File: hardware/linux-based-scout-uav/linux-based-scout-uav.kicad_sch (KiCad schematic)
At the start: 0 parts

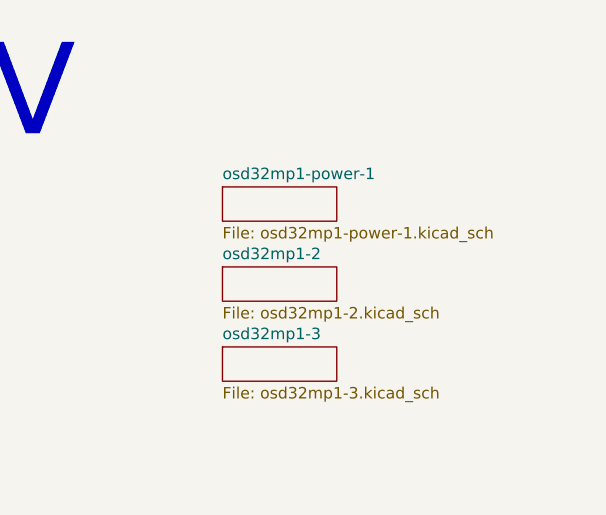
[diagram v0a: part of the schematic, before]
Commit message: Schematic update
Schematic updates on battery connector and OSD32MP1 power section.
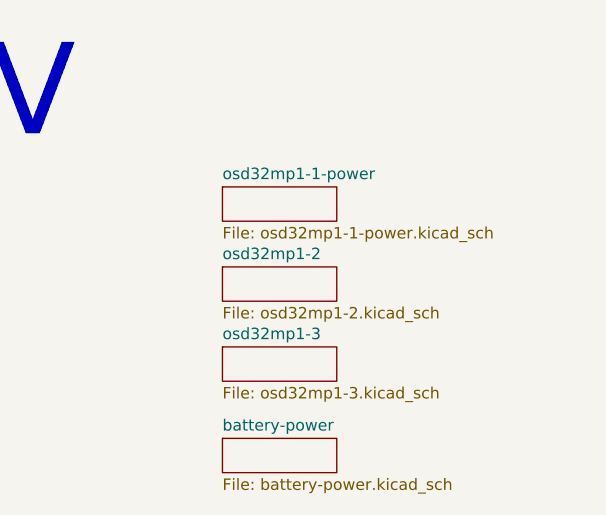
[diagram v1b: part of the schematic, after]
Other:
- sheet osd32mp1-power-1 renamed osd32mp1-1-power
- added sheet battery-power (battery-power.kicad_sch)
- sheet osd32mp1-1-power: file osd32mp1-power-1.kicad_sch -> osd32mp1-1-power.kicad_sch
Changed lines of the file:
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@@
+	)
+	(sheet
+		(at 242.57 59.69)
+		(size 12.7 3.81)
+		(fields_autoplaced yes)
+		(stroke
+			(width 0.1524)
+			(type solid)
+		)
+		(fill
+			(color 0 0 0 0.0000)
+		)
+		(property "Sheetname" "battery-power"
+			(at 242.57 58.9784 0)
+			(show_name yes)
+			(effects
+				(font
+					(size 1.27 1.27)
+				)
+				(justify left bottom)
+			)
+		)
+		(property "Sheetfile" "battery-power.kicad_sch"
+			(at 242.57 64.0846 0)
+			(effects
+				(font
+					(size 1.27 1.27)
+				)
+				(justify left top)
+			)
+		)
+		(instances
+			(project "linux-based-scout-uav"
+				(path "/e9b29a7c-bbe5-4ab4-acee-985586e1266a"
+					(page "5")
+				)
+			)
+		)
 	)
 	(sheet
@@
 			(color 0 0 0 0.0000)
 		)
-		(property "Sheetname" "osd32mp1-power-1"
+		(property "Sheetname" "osd32mp1-1-power"
 			(at 242.57 31.0384 0)
 			(show_name yes)
@@
 			)
 		)
-		(property "Sheetfile" "osd32mp1-power-1.kicad_sch"
+		(property "Sheetfile" "osd32mp1-1-power.kicad_sch"
 			(at 242.57 36.1446 0)
 			(effects

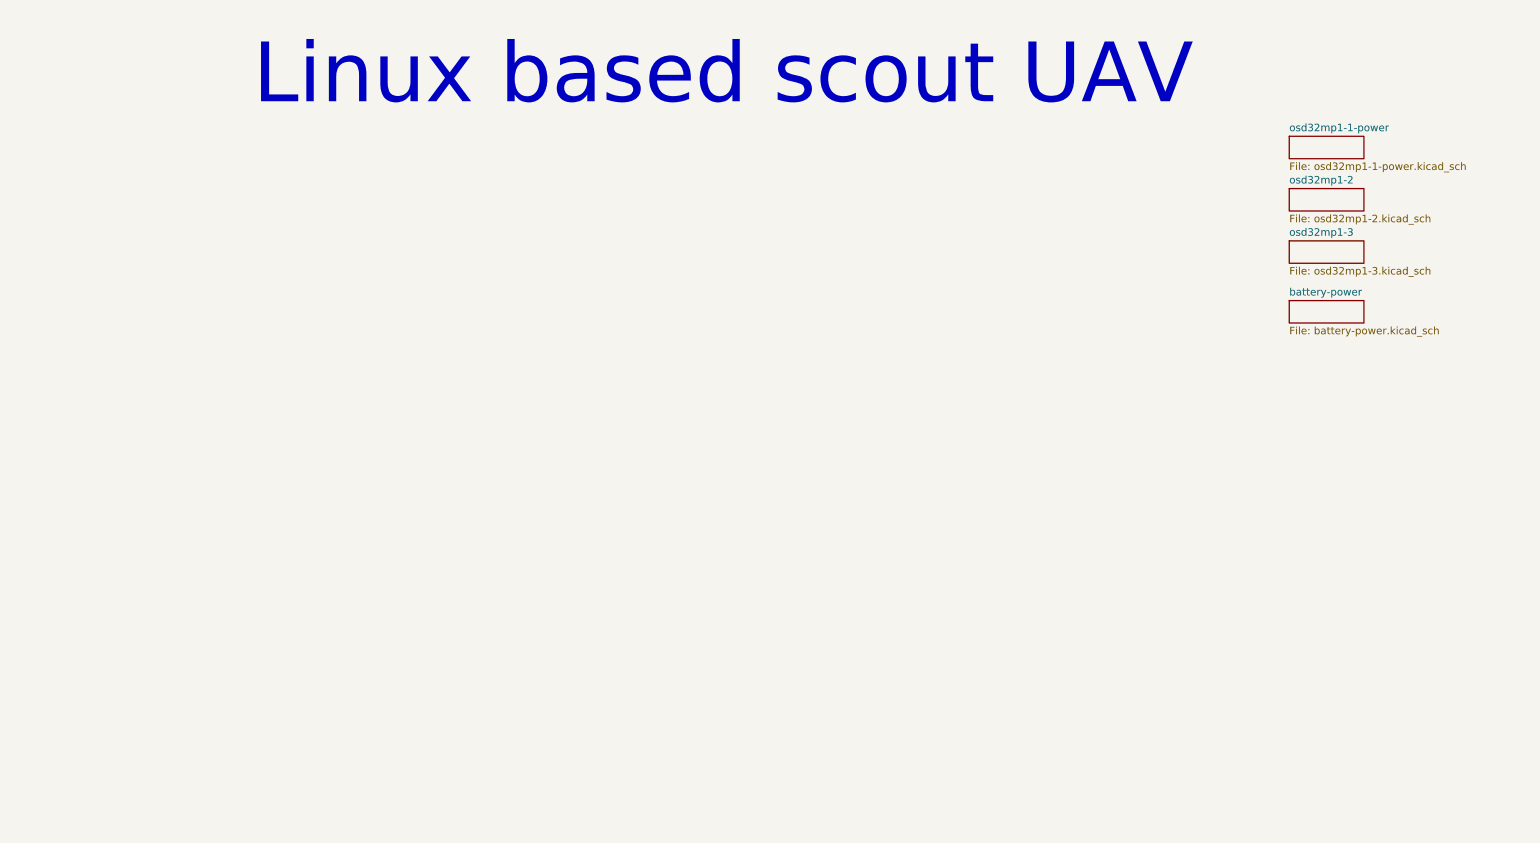
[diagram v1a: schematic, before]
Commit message: Updates (Schematic, Readme, doc)
Updates to Schematic capture, README file and doc files.
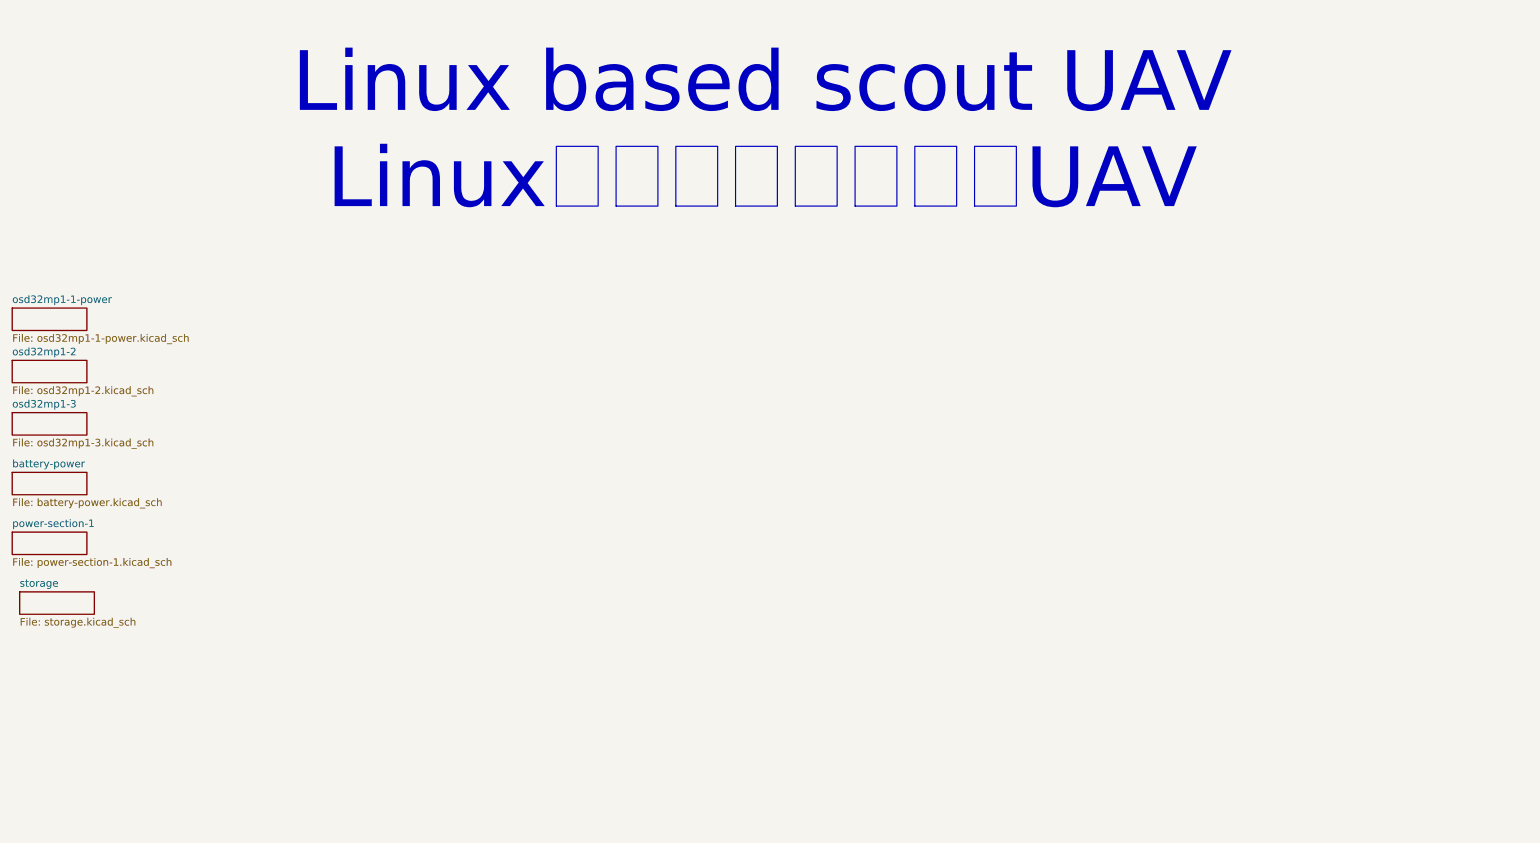
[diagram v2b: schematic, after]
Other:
- added sheet power-section-1 (power-section-1.kicad_sch)
- added sheet storage (storage.kicad_sch)
- note added: "Linux based scout UAV LinuxベースのスカウトUAV"
- note removed: "Linux based scout UAV"
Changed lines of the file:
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@@
 	(generator_version "8.0")
 	(paper "A4")
-	(text "Linux based scout UAV"
+	(text "Linux based scout UAV\nLinuxベースのスカウトUAV"
 		(exclude_from_sim no)
-		(at 146.304 21.336 0)
+		(at 152.908 30.988 0)
 		(effects
 			(font
@@
 	)
 	(sheet
-		(at 242.57 49.53)
+		(at 25.4 78.74)
 		(size 12.7 3.81)
 		(fields_autoplaced yes)
@@
 		)
 		(property "Sheetname" "osd32mp1-3"
-			(at 242.57 48.8184 0)
+			(at 25.4 78.0284 0)
 			(show_name yes)
 			(effects
@@
 		)
 		(property "Sheetfile" "osd32mp1-3.kicad_sch"
-			(at 242.57 53.9246 0)
+			(at 25.4 83.1346 0)
 			(effects
 				(font
@@
 	)
 	(sheet
-		(at 242.57 59.69)
+		(at 25.4 88.9)
 		(size 12.7 3.81)
 		(fields_autoplaced yes)
@@
 		)
 		(property "Sheetname" "battery-power"
-			(at 242.57 58.9784 0)
+			(at 25.4 88.1884 0)
 			(show_name yes)
 			(effects
@@
 		)
 		(property "Sheetfile" "battery-power.kicad_sch"
-			(at 242.57 64.0846 0)
+			(at 25.4 93.2946 0)
 			(effects
 				(font
@@
 	)
 	(sheet
-		(at 242.57 31.75)
+		(at 25.4 99.06)
+		(size 12.7 3.81)
+		(fields_autoplaced yes)
+		(stroke
+			(width 0.1524)
+			(type solid)
+		)
+		(fill
+			(color 0 0 0 0.0000)
+		)
+		(property "Sheetname" "power-section-1"
+			(at 25.4 98.3484 0)
+			(show_name yes)
+			(effects
+				(font
+					(size 1.27 1.27)
+				)
+				(justify left bottom)
+			)
+		)
+		(property "Sheetfile" "power-section-1.kicad_sch"
+			(at 25.4 103.4546 0)
+			(effects
+				(font
+					(size 1.27 1.27)
+				)
+				(justify left top)
+			)
+		)
+		(instances
+			(project "linux-based-scout-uav"
+				(path "/e9b29a7c-bbe5-4ab4-acee-985586e1266a"
+					(page "6")
+				)
+			)
+		)
+	)
+	(sheet
+		(at 25.4 60.96)
 		(size 12.7 3.81)
 		(fields_autoplaced yes)
@@
 		)
 		(property "Sheetname" "osd32mp1-1-power"
-			(at 242.57 31.0384 0)
+			(at 25.4 60.2484 0)
 			(show_name yes)
 			(effects
@@
 		)
 		(property "Sheetfile" "osd32mp1-1-power.kicad_sch"
-			(at 242.57 36.1446 0)
+			(at 25.4 65.3546 0)
 			(effects
 				(font
@@
 	)
 	(sheet
-		(at 242.57 40.64)
+		(at 25.4 69.85)
 		(size 12.7 3.81)
 		(fields_autoplaced yes)
@@
 		)
 		(property "Sheetname" "osd32mp1-2"
-			(at 242.57 39.9284 0)
+			(at 25.4 69.1384 0)
 			(show_name yes)
 			(effects
@@
 		)
 		(property "Sheetfile" "osd32mp1-2.kicad_sch"
-			(at 242.57 45.0346 0)
+			(at 25.4 74.2446 0)
 			(effects
 				(font
@@
 				)
 			)
+		)
+	)
+	(sheet
+		(at 26.67 109.22)
+		(size 12.7 3.81)
+		(fields_autoplaced yes)
+		(stroke
+			(width 0.1524)
+			(type solid)
+		)
+		(fill
+			(color 0 0 0 0.0000)
+		)
+		(property "Sheetname" "storage"
+			(at 26.67 108.5084 0)
+			(effects
+				(font
+					(size 1.27 1.27)
+				)
+				(justify left bottom)
+			)
+		)
+		(property "Sheetfile" "storage.kicad_sch"
+			(at 26.67 113.6146 0)
+			(effects
+				(font
+					(size 1.27 1.27)
+				)
+				(justify left top)
+			)
+		)
+		(instances
+			(project "linux-based-scout-uav"
+				(path "/e9b29a7c-bbe5-4ab4-acee-985586e1266a"
+					(page "7")
+				)
+			)

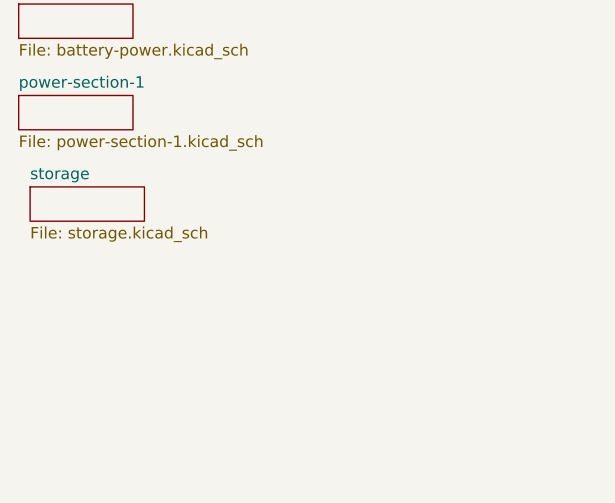
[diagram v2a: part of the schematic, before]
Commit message: Schematic, board update
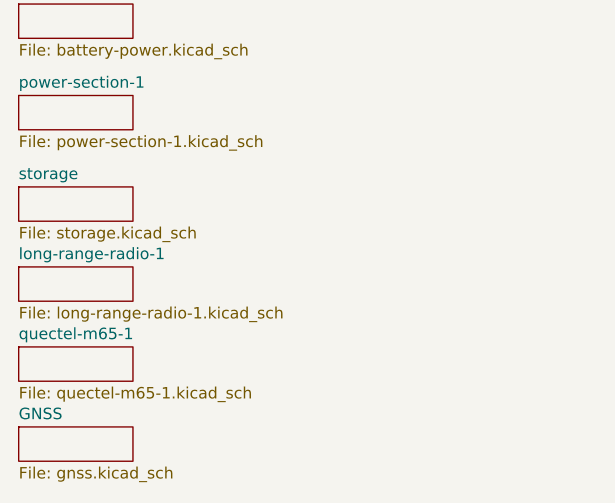
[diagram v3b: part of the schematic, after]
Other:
- added sheet GNSS (gnss.kicad_sch)
- added sheet long-range-radio-1 (long-range-radio-1.kicad_sch)
- added sheet quectel-m65-1 (quectel-m65-1.kicad_sch)
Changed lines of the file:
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@@
+	)
+	(sheet
+		(at 25.4 127)
+		(size 12.7 3.81)
+		(fields_autoplaced yes)
+		(stroke
+			(width 0.1524)
+			(type solid)
+		)
+		(fill
+			(color 0 0 0 0.0000)
+		)
+		(property "Sheetname" "quectel-m65-1"
+			(at 25.4 126.2884 0)
+			(effects
+				(font
+					(size 1.27 1.27)
+				)
+				(justify left bottom)
+			)
+		)
+		(property "Sheetfile" "quectel-m65-1.kicad_sch"
+			(at 25.4 131.3946 0)
+			(effects
+				(font
+					(size 1.27 1.27)
+				)
+				(justify left top)
+			)
+		)
+		(instances
+			(project "linux-based-scout-uav"
+				(path "/e9b29a7c-bbe5-4ab4-acee-985586e1266a"
+					(page "9")
+				)
+			)
+		)
 	)
 	(sheet
@@
 	)
 	(sheet
+		(at 25.4 135.89)
+		(size 12.7 3.81)
+		(fields_autoplaced yes)
+		(stroke
+			(width 0.1524)
+			(type solid)
+		)
+		(fill
+			(color 0 0 0 0.0000)
+		)
+		(property "Sheetname" "GNSS"
+			(at 25.4 135.1784 0)
+			(effects
+				(font
+					(size 1.27 1.27)
+				)
+				(justify left bottom)
+			)
+		)
+		(property "Sheetfile" "gnss.kicad_sch"
+			(at 25.4 140.2846 0)
+			(effects
+				(font
+					(size 1.27 1.27)
+				)
+				(justify left top)
+			)
+		)
+		(instances
+			(project "linux-based-scout-uav"
+				(path "/e9b29a7c-bbe5-4ab4-acee-985586e1266a"
+					(page "10")
+				)
+			)
+		)
+	)
+	(sheet
 		(at 25.4 69.85)
 		(size 12.7 3.81)
@@
 	)
 	(sheet
-		(at 26.67 109.22)
+		(at 25.4 118.11)
+		(size 12.7 3.81)
+		(fields_autoplaced yes)
+		(stroke
+			(width 0.1524)
+			(type solid)
+		)
+		(fill
+			(color 0 0 0 0.0000)
+		)
+		(property "Sheetname" "long-range-radio-1"
+			(at 25.4 117.3984 0)
+			(effects
+				(font
+					(size 1.27 1.27)
+				)
+				(justify left bottom)
+			)
+		)
+		(property "Sheetfile" "long-range-radio-1.kicad_sch"
+			(at 25.4 122.5046 0)
+			(effects
+				(font
+					(size 1.27 1.27)
+				)
+				(justify left top)
+			)
+		)
+		(instances
+			(project "linux-based-scout-uav"
+				(path "/e9b29a7c-bbe5-4ab4-acee-985586e1266a"
+					(page "8")
+				)
+			)
+		)
+	)
+	(sheet
+		(at 25.4 109.22)
 		(size 12.7 3.81)
 		(fields_autoplaced yes)
@@
 		)
 		(property "Sheetname" "storage"
-			(at 26.67 108.5084 0)
+			(at 25.4 108.5084 0)
 			(effects
 				(font
@@
 		)
 		(property "Sheetfile" "storage.kicad_sch"
-			(at 26.67 113.6146 0)
-			(effects
-				(font
+			(at 25.4 113.6146 0)
+			(effects
+				(font

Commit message: Schematic update
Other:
- added sheet sensors-1 (sensors-1.kicad_sch)
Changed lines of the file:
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@@
+	)
+	(sheet
+		(at 25.4 143.51)
+		(size 12.7 3.81)
+		(fields_autoplaced yes)
+		(stroke
+			(width 0.1524)
+			(type solid)
+		)
+		(fill
+			(color 0 0 0 0.0000)
+		)
+		(property "Sheetname" "sensors-1"
+			(at 25.4 142.7984 0)
+			(effects
+				(font
+					(size 1.27 1.27)
+				)
+				(justify left bottom)
+			)
+		)
+		(property "Sheetfile" "sensors-1.kicad_sch"
+			(at 25.4 147.9046 0)
+			(effects
+				(font
+					(size 1.27 1.27)
+				)
+				(justify left top)
+			)
+		)
+		(instances
+			(project "linux-based-scout-uav"
+				(path "/e9b29a7c-bbe5-4ab4-acee-985586e1266a"
+					(page "11")
+				)
+			)
+		)
 	)
 	(sheet
